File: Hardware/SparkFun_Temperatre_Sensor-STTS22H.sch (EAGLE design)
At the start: 26 parts, among them J1 QWIIC_RIGHT_ANGLE, J2 QWIIC_RIGHT_ANGLE, U2 STTS22H

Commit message: Removes ADDR pin from header
* Routes board
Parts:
- added STANDOFF3: STAND-OFFTIGHT, SparkFun-Hardware:STAND-OFFTIGHT
- J3: device SparkFun-Connectors:CONN_06NO_SILK_NO_POP -> SparkFun-Connectors:CONN_05NO_SILK
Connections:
- net !INT!: now also J3.5; no longer J3.6
- net ADDR: no longer J3.5
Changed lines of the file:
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@@
 <part name="FD4" library="SparkFun-Aesthetics" deviceset="FIDUCIAL" device="1X2"/>
 <part name="LOGO4" library="SparkFun-Aesthetics" deviceset="QWIIC_LOGO" device="_4MM"/>
-<part name="J3" library="SparkFun-Connectors" deviceset="CONN_06" device="NO_SILK_NO_POP"/>
+<part name="J3" library="SparkFun-Connectors" deviceset="CONN_05" device="NO_SILK"/>
 <part name="ADDR" library="SparkFun-Jumpers" deviceset="JUMPER-SMT_3_1-NC_TRACE" device="_SILK" package3d_urn="urn:adsk.eagle:package:39288/1"/>
 <part name="R7" library="SparkFun-Resistors" deviceset="56KOHM" device="" value="56k"/>
@@
 <part name="SUPPLY8" library="SparkFun-PowerSymbols" deviceset="3.3V" device=""/>
 <part name="GND2" library="SparkFun-PowerSymbols" deviceset="GND" device=""/>
+<part name="STANDOFF3" library="SparkFun-Hardware" deviceset="STAND-OFF" device="TIGHT"/>
 </parts>
 <sheets>
@@
 <instance part="FD4" gate="G$1" x="243.84" y="27.94" smashed="yes"/>
 <instance part="LOGO4" gate="G$1" x="180.34" y="40.64" smashed="yes"/>
-<instance part="J3" gate="JP1" x="17.78" y="20.32" smashed="yes">
-<attribute name="VALUE" x="12.7" y="10.414" size="1.778" layer="96" font="vector"/>
-<attribute name="NAME" x="12.7" y="33.528" size="1.778" layer="95" font="vector"/>
+<instance part="J3" gate="G$1" x="15.24" y="20.32" smashed="yes">
+<attribute name="VALUE" x="10.16" y="10.414" size="1.778" layer="96" font="vector"/>
+<attribute name="NAME" x="12.7" y="28.448" size="1.778" layer="95" font="vector"/>
 </instance>
 <instance part="ADDR" gate="G$1" x="25.4" y="101.6" smashed="yes" rot="MR90">
@@
 <attribute name="VALUE" x="104.14" y="96.266" size="1.778" layer="96" font="vector" align="top-center"/>
 </instance>
+<instance part="STANDOFF3" gate="G$1" x="241.3" y="30.48" smashed="yes"/>
 </instances>
 <busses>
@@
 <net name="GND" class="0">
 <segment>
+<pinref part="GND11" gate="1" pin="GND"/>
 <wire x1="22.86" y1="15.24" x2="25.4" y2="15.24" width="0.1524" layer="91"/>
-<pinref part="GND11" gate="1" pin="GND"/>
 <wire x1="25.4" y1="15.24" x2="25.4" y2="12.7" width="0.1524" layer="91"/>
-<pinref part="J3" gate="JP1" pin="1"/>
+<pinref part="J3" gate="G$1" pin="1"/>
 </segment>
 <segment>
@@
 <net name="3.3V" class="0">
 <segment>
+<pinref part="SUPPLY6" gate="G$1" pin="3.3V"/>
 <wire x1="22.86" y1="17.78" x2="25.4" y2="17.78" width="0.1524" layer="91"/>
-<pinref part="SUPPLY6" gate="G$1" pin="3.3V"/>
 <wire x1="25.4" y1="17.78" x2="25.4" y2="38.1" width="0.1524" layer="91"/>
-<pinref part="J3" gate="JP1" pin="2"/>
+<pinref part="J3" gate="G$1" pin="2"/>
 </segment>
 <segment>
@@
 </segment>
 <segment>
-<pinref part="J3" gate="JP1" pin="6"/>
-<wire x1="27.94" y1="27.94" x2="22.86" y2="27.94" width="0.1524" layer="91"/>
-<label x="27.94" y="27.94" size="1.27" layer="95" font="vector" xref="yes"/>
+<wire x1="27.94" y1="25.4" x2="22.86" y2="25.4" width="0.1524" layer="91"/>
+<label x="27.94" y="25.4" size="1.27" layer="95" font="vector" xref="yes"/>
+<pinref part="J3" gate="G$1" pin="5"/>
 </segment>
 </net>
@@
 </segment>
 <segment>
-<pinref part="J3" gate="JP1" pin="5"/>
-<wire x1="27.94" y1="25.4" x2="22.86" y2="25.4" width="0.1524" layer="91"/>
-<label x="27.94" y="25.4" size="1.27" layer="95" font="vector" xref="yes"/>
-</segment>
-<segment>
 <pinref part="ADDR" gate="G$1" pin="2"/>
 <wire x1="22.86" y1="93.98" x2="25.4" y2="93.98" width="0.1524" layer="91"/>
@@
 <wire x1="22.86" y1="22.86" x2="27.94" y2="22.86" width="0.1524" layer="91"/>
 <label x="27.94" y="22.86" size="1.27" layer="95" font="vector" xref="yes"/>
-<pinref part="J3" gate="JP1" pin="4"/>
+<pinref part="J3" gate="G$1" pin="4"/>
 </segment>
 <segment>
@@
 <wire x1="22.86" y1="20.32" x2="27.94" y2="20.32" width="0.1524" layer="91"/>
 <label x="27.94" y="20.32" size="1.27" layer="95" font="vector" xref="yes"/>
-<pinref part="J3" gate="JP1" pin="3"/>
-</segment>
-<segment>
+<pinref part="J3" gate="G$1" pin="3"/>
+</segment>
+<segment>

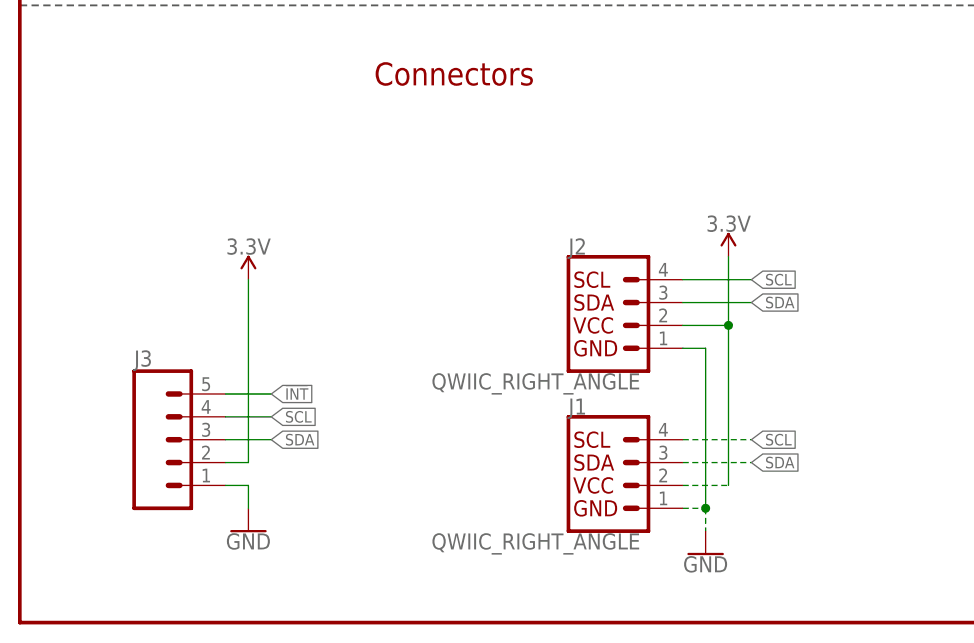
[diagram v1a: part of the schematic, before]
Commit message: Adds silk
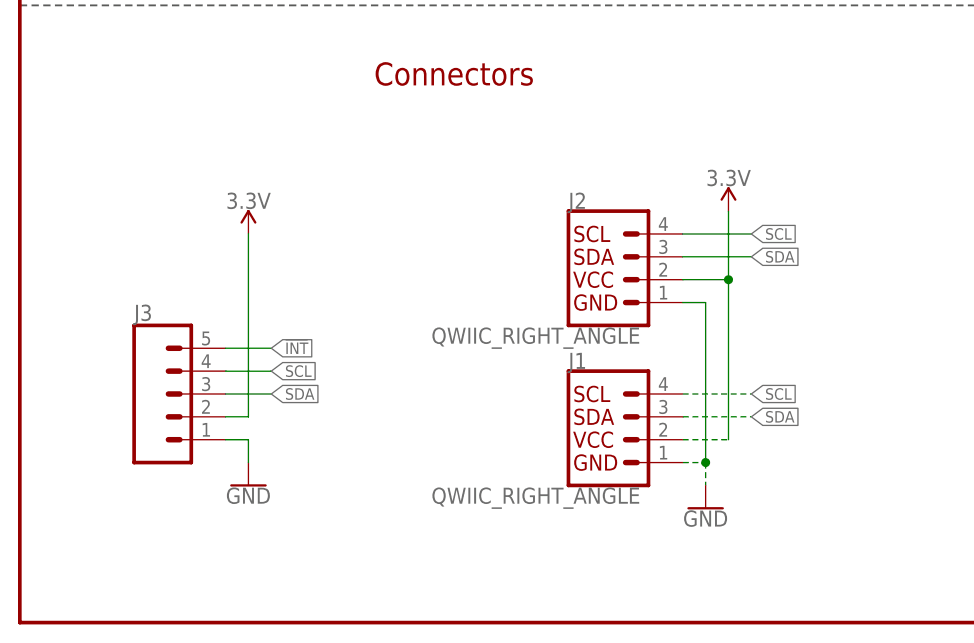
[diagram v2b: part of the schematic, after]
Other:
- moved on the sheet: J1, J2, J3
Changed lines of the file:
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@@
 <attribute name="VALUE" x="167.64" y="132.334" size="1.778" layer="96" font="vector" align="bottom-center"/>
 </instance>
-<instance part="SUPPLY6" gate="G$1" x="25.4" y="38.1" smashed="yes">
-<attribute name="VALUE" x="25.4" y="40.894" size="1.778" layer="96" font="vector" align="bottom-center"/>
-</instance>
-<instance part="GND11" gate="1" x="25.4" y="10.16" smashed="yes">
-<attribute name="VALUE" x="25.4" y="9.906" size="1.778" layer="96" font="vector" align="top-center"/>
+<instance part="SUPPLY6" gate="G$1" x="25.4" y="43.18" smashed="yes">
+<attribute name="VALUE" x="25.4" y="45.974" size="1.778" layer="96" font="vector" align="bottom-center"/>
+</instance>
+<instance part="GND11" gate="1" x="25.4" y="15.24" smashed="yes">
+<attribute name="VALUE" x="25.4" y="14.986" size="1.778" layer="96" font="vector" align="top-center"/>
 </instance>
 <instance part="I2C_PU" gate="G$1" x="167.64" y="121.92" smashed="yes" rot="MR270">
@@
 </instance>
 <instance part="LOGO3" gate="G$1" x="190.5" y="33.02" smashed="yes"/>
-<instance part="J1" gate="G$1" x="66.04" y="15.24" smashed="yes">
-<attribute name="VALUE" x="45.72" y="9.906" size="1.778" layer="96" font="vector" align="top-left"/>
-<attribute name="NAME" x="60.96" y="23.114" size="1.778" layer="95" font="vector"/>
-</instance>
-<instance part="SUPPLY1" gate="G$1" x="78.74" y="40.64" smashed="yes">
-<attribute name="VALUE" x="78.74" y="43.434" size="1.778" layer="96" font="vector" align="bottom-center"/>
-</instance>
-<instance part="GND3" gate="1" x="76.2" y="7.62" smashed="yes">
-<attribute name="VALUE" x="76.2" y="7.366" size="1.778" layer="96" font="vector" align="top-center"/>
-</instance>
-<instance part="J2" gate="G$1" x="66.04" y="33.02" smashed="yes">
-<attribute name="VALUE" x="45.72" y="27.686" size="1.778" layer="96" font="vector" align="top-left"/>
-<attribute name="NAME" x="60.96" y="40.894" size="1.778" layer="95" font="vector"/>
+<instance part="J1" gate="G$1" x="66.04" y="20.32" smashed="yes">
+<attribute name="VALUE" x="45.72" y="14.986" size="1.778" layer="96" font="vector" align="top-left"/>
+<attribute name="NAME" x="60.96" y="28.194" size="1.778" layer="95" font="vector"/>
+</instance>
+<instance part="SUPPLY1" gate="G$1" x="78.74" y="45.72" smashed="yes">
+<attribute name="VALUE" x="78.74" y="48.514" size="1.778" layer="96" font="vector" align="bottom-center"/>
+</instance>
+<instance part="GND3" gate="1" x="76.2" y="12.7" smashed="yes">
+<attribute name="VALUE" x="76.2" y="12.446" size="1.778" layer="96" font="vector" align="top-center"/>
+</instance>
+<instance part="J2" gate="G$1" x="66.04" y="38.1" smashed="yes">
+<attribute name="VALUE" x="45.72" y="32.766" size="1.778" layer="96" font="vector" align="top-left"/>
+<attribute name="NAME" x="60.96" y="45.974" size="1.778" layer="95" font="vector"/>
 </instance>
 <instance part="D1" gate="G$1" x="203.2" y="127" smashed="yes">
@@
 <instance part="FD4" gate="G$1" x="243.84" y="27.94" smashed="yes"/>
 <instance part="LOGO4" gate="G$1" x="180.34" y="40.64" smashed="yes"/>
-<instance part="J3" gate="G$1" x="15.24" y="20.32" smashed="yes">
-<attribute name="VALUE" x="10.16" y="10.414" size="1.778" layer="96" font="vector"/>
-<attribute name="NAME" x="12.7" y="28.448" size="1.778" layer="95" font="vector"/>
+<instance part="J3" gate="G$1" x="15.24" y="25.4" smashed="yes">
+<attribute name="VALUE" x="10.16" y="15.494" size="1.778" layer="96" font="vector"/>
+<attribute name="NAME" x="12.7" y="33.528" size="1.778" layer="95" font="vector"/>
 </instance>
 <instance part="ADDR" gate="G$1" x="25.4" y="101.6" smashed="yes" rot="MR90">
@@
 <segment>
 <pinref part="GND11" gate="1" pin="GND"/>
-<wire x1="22.86" y1="15.24" x2="25.4" y2="15.24" width="0.1524" layer="91"/>
-<wire x1="25.4" y1="15.24" x2="25.4" y2="12.7" width="0.1524" layer="91"/>
+<wire x1="22.86" y1="20.32" x2="25.4" y2="20.32" width="0.1524" layer="91"/>
+<wire x1="25.4" y1="20.32" x2="25.4" y2="17.78" width="0.1524" layer="91"/>
 <pinref part="J3" gate="G$1" pin="1"/>
 </segment>
 <segment>
 <pinref part="J1" gate="G$1" pin="1"/>
-<wire x1="73.66" y1="12.7" x2="76.2" y2="12.7" width="0.1524" layer="91" style="longdash"/>
-<wire x1="76.2" y1="12.7" x2="76.2" y2="10.16" width="0.1524" layer="91" style="longdash"/>
+<wire x1="73.66" y1="17.78" x2="76.2" y2="17.78" width="0.1524" layer="91" style="longdash"/>
+<wire x1="76.2" y1="17.78" x2="76.2" y2="15.24" width="0.1524" layer="91" style="longdash"/>
 <pinref part="GND3" gate="1" pin="GND"/>
 <pinref part="J2" gate="G$1" pin="1"/>
-<wire x1="73.66" y1="30.48" x2="76.2" y2="30.48" width="0.1524" layer="91"/>
-<wire x1="76.2" y1="30.48" x2="76.2" y2="12.7" width="0.1524" layer="91"/>
-<junction x="76.2" y="12.7"/>
+<wire x1="73.66" y1="35.56" x2="76.2" y2="35.56" width="0.1524" layer="91"/>
+<wire x1="76.2" y1="35.56" x2="76.2" y2="17.78" width="0.1524" layer="91"/>
+<junction x="76.2" y="17.78"/>
 </segment>
 <segment>
@@
 <segment>
 <pinref part="SUPPLY6" gate="G$1" pin="3.3V"/>
-<wire x1="22.86" y1="17.78" x2="25.4" y2="17.78" width="0.1524" layer="91"/>
-<wire x1="25.4" y1="17.78" x2="25.4" y2="38.1" width="0.1524" layer="91"/>
+<wire x1="22.86" y1="22.86" x2="25.4" y2="22.86" width="0.1524" layer="91"/>
+<wire x1="25.4" y1="22.86" x2="25.4" y2="43.18" width="0.1524" layer="91"/>
 <pinref part="J3" gate="G$1" pin="2"/>
 </segment>
@@
 <segment>
 <pinref part="J1" gate="G$1" pin="2"/>
-<wire x1="73.66" y1="15.24" x2="78.74" y2="15.24" width="0.1524" layer="91" style="longdash"/>
-<wire x1="78.74" y1="15.24" x2="78.74" y2="33.02" width="0.1524" layer="91"/>
+<wire x1="73.66" y1="20.32" x2="78.74" y2="20.32" width="0.1524" layer="91" style="longdash"/>
+<wire x1="78.74" y1="20.32" x2="78.74" y2="38.1" width="0.1524" layer="91"/>
 <pinref part="SUPPLY1" gate="G$1" pin="3.3V"/>
 <pinref part="J2" gate="G$1" pin="2"/>
-<wire x1="78.74" y1="33.02" x2="78.74" y2="40.64" width="0.1524" layer="91"/>
-<wire x1="73.66" y1="33.02" x2="78.74" y2="33.02" width="0.1524" layer="91"/>
-<junction x="78.74" y="33.02"/>
+<wire x1="78.74" y1="38.1" x2="78.74" y2="45.72" width="0.1524" layer="91"/>
+<wire x1="73.66" y1="38.1" x2="78.74" y2="38.1" width="0.1524" layer="91"/>
+<junction x="78.74" y="38.1"/>
 </segment>
 <segment>
@@
 </segment>
 <segment>
-<wire x1="27.94" y1="25.4" x2="22.86" y2="25.4" width="0.1524" layer="91"/>
-<label x="27.94" y="25.4" size="1.27" layer="95" font="vector" xref="yes"/>
+<wire x1="27.94" y1="30.48" x2="22.86" y2="30.48" width="0.1524" layer="91"/>
+<label x="27.94" y="30.48" size="1.27" layer="95" font="vector" xref="yes"/>
 <pinref part="J3" gate="G$1" pin="5"/>
 </segment>
@@
 </segment>
 <segment>
-<wire x1="22.86" y1="22.86" x2="27.94" y2="22.86" width="0.1524" layer="91"/>
-<label x="27.94" y="22.86" size="1.27" layer="95" font="vector" xref="yes"/>
+<wire x1="22.86" y1="27.94" x2="27.94" y2="27.94" width="0.1524" layer="91"/>
+<label x="27.94" y="27.94" size="1.27" layer="95" font="vector" xref="yes"/>
 <pinref part="J3" gate="G$1" pin="4"/>
 </segment>
 <segment>
 <pinref part="J1" gate="G$1" pin="4"/>
-<wire x1="73.66" y1="20.32" x2="81.28" y2="20.32" width="0.1524" layer="91" style="longdash"/>
-<label x="81.28" y="20.32" size="1.27" layer="95" font="vector" xref="yes"/>
+<wire x1="73.66" y1="25.4" x2="81.28" y2="25.4" width="0.1524" layer="91" style="longdash"/>
+<label x="81.28" y="25.4" size="1.27" layer="95" font="vector" xref="yes"/>
 </segment>
 <segment>
@@
 <segment>
 <pinref part="J2" gate="G$1" pin="4"/>
-<wire x1="73.66" y1="38.1" x2="81.28" y2="38.1" width="0.1524" layer="91"/>
-<label x="81.28" y="38.1" size="1.27" layer="95" font="vector" xref="yes"/>
+<wire x1="73.66" y1="43.18" x2="81.28" y2="43.18" width="0.1524" layer="91"/>
+<label x="81.28" y="43.18" size="1.27" layer="95" font="vector" xref="yes"/>
 </segment>
 </net>
@@
 </segment>
 <segment>
-<wire x1="22.86" y1="20.32" x2="27.94" y2="20.32" width="0.1524" layer="91"/>
-<label x="27.94" y="20.32" size="1.27" layer="95" font="vector" xref="yes"/>
+<wire x1="22.86" y1="25.4" x2="27.94" y2="25.4" width="0.1524" layer="91"/>
+<label x="27.94" y="25.4" size="1.27" layer="95" font="vector" xref="yes"/>
 <pinref part="J3" gate="G$1" pin="3"/>
 </segment>
 <segment>
 <pinref part="J1" gate="G$1" pin="3"/>
-<wire x1="73.66" y1="17.78" x2="81.28" y2="17.78" width="0.1524" layer="91" style="longdash"/>
-<label x="81.28" y="17.78" size="1.27" layer="95" font="vector" xref="yes"/>
+<wire x1="73.66" y1="22.86" x2="81.28" y2="22.86" width="0.1524" layer="91" style="longdash"/>
+<label x="81.28" y="22.86" size="1.27" layer="95" font="vector" xref="yes"/>
 </segment>
 <segment>
@@
 <segment>
 <pinref part="J2" gate="G$1" pin="3"/>
-<wire x1="73.66" y1="35.56" x2="81.28" y2="35.56" width="0.1524" layer="91"/>
-<label x="81.28" y="35.56" size="1.27" layer="95" font="vector" xref="yes"/>
-</segment>
-</net>
+<wire x1="73.66" y1="40.64" x2="81.28" y2="40.64" width="0.1524" layer="91"/>
+<label x="81.28" y="40.64" size="1.27" layer="95" font="vector" xref="yes"/>
+</segment>
+</net>

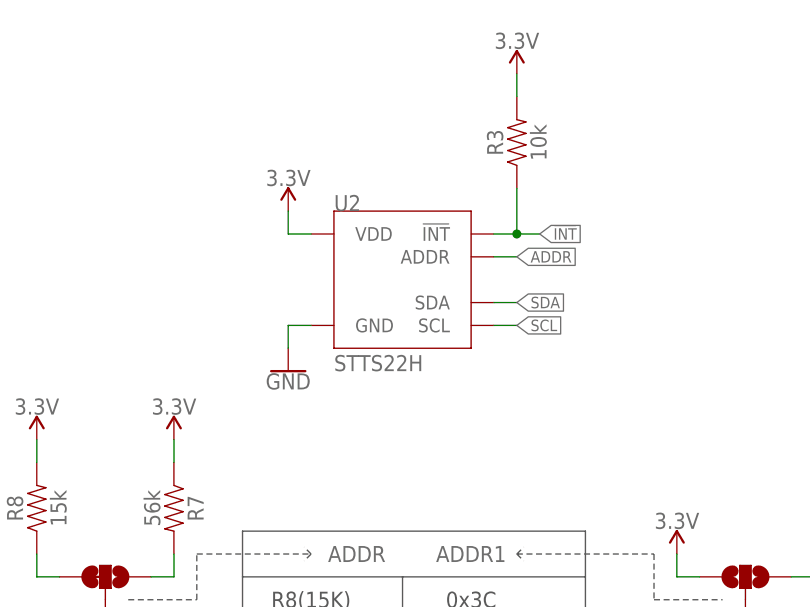
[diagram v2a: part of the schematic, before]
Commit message: Adds decoupling cap which resulted in additional routing
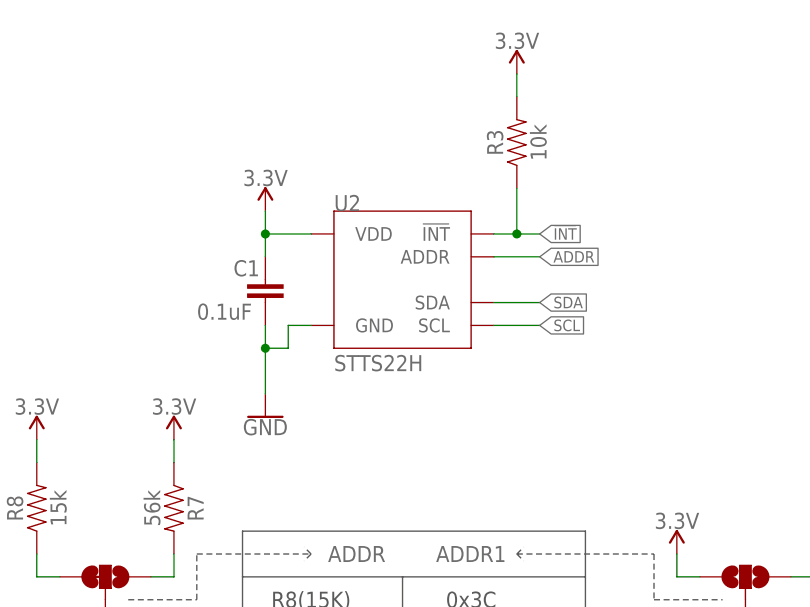
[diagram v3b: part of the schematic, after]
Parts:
- added C1: 0.1uF, SparkFun-Capacitors:0.1UF-0603-25V-(+80/-20%)
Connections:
- net 3.3V: now also C1.1
- net GND: now also C1.2
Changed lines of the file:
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@@
 <part name="GND2" library="SparkFun-PowerSymbols" deviceset="GND" device=""/>
 <part name="STANDOFF3" library="SparkFun-Hardware" deviceset="STAND-OFF" device="TIGHT"/>
+<part name="C1" library="SparkFun-Capacitors" deviceset="0.1UF" device="-0603-25V-(+80/-20%)" value="0.1uF"/>
 </parts>
 <sheets>
@@
 <attribute name="VALUE" x="50.8" y="124.46" size="1.778" layer="96" font="vector"/>
 </instance>
-<instance part="SUPPLY4" gate="G$1" x="45.72" y="142.24" smashed="yes">
-<attribute name="VALUE" x="45.72" y="145.034" size="1.778" layer="96" font="vector" align="bottom-center"/>
-</instance>
-<instance part="GND1" gate="1" x="45.72" y="124.46" smashed="yes">
-<attribute name="VALUE" x="45.72" y="124.206" size="1.778" layer="96" font="vector" align="top-center"/>
+<instance part="SUPPLY4" gate="G$1" x="43.18" y="142.24" smashed="yes">
+<attribute name="VALUE" x="43.18" y="145.034" size="1.778" layer="96" font="vector" align="bottom-center"/>
+</instance>
+<instance part="GND1" gate="1" x="43.18" y="119.38" smashed="yes">
+<attribute name="VALUE" x="43.18" y="119.126" size="1.778" layer="96" font="vector" align="top-center"/>
 </instance>
 <instance part="R3" gate="G$1" x="71.12" y="149.86" smashed="yes" rot="R90">
@@
 </instance>
 <instance part="STANDOFF3" gate="G$1" x="241.3" y="30.48" smashed="yes"/>
+<instance part="C1" gate="G$1" x="43.18" y="132.08" smashed="yes">
+<attribute name="NAME" x="39.624" y="135.001" size="1.778" layer="95" font="vector"/>
+<attribute name="VALUE" x="35.56" y="130.175" size="1.778" layer="96" font="vector"/>
+</instance>
 </instances>
 <busses>
@@
 <segment>
 <pinref part="U2" gate="G$1" pin="GND"/>
+<wire x1="43.18" y1="121.92" x2="43.18" y2="127" width="0.1524" layer="91"/>
+<wire x1="43.18" y1="127" x2="45.72" y2="127" width="0.1524" layer="91"/>
 <wire x1="45.72" y1="127" x2="45.72" y2="129.54" width="0.1524" layer="91"/>
 <wire x1="45.72" y1="129.54" x2="48.26" y2="129.54" width="0.1524" layer="91"/>
 <pinref part="GND1" gate="1" pin="GND"/>
+<pinref part="C1" gate="G$1" pin="2"/>
+<wire x1="43.18" y1="129.54" x2="43.18" y2="127" width="0.1524" layer="91"/>
+<junction x="43.18" y="127"/>
 </segment>
 <segment>
@@
 <segment>
 <pinref part="U2" gate="G$1" pin="VDD"/>
-<wire x1="45.72" y1="142.24" x2="45.72" y2="139.7" width="0.1524" layer="91"/>
-<wire x1="45.72" y1="139.7" x2="48.26" y2="139.7" width="0.1524" layer="91"/>
+<wire x1="43.18" y1="142.24" x2="43.18" y2="139.7" width="0.1524" layer="91"/>
+<wire x1="43.18" y1="139.7" x2="48.26" y2="139.7" width="0.1524" layer="91"/>
 <pinref part="SUPPLY4" gate="G$1" pin="3.3V"/>
+<pinref part="C1" gate="G$1" pin="1"/>
+<wire x1="43.18" y1="137.16" x2="43.18" y2="139.7" width="0.1524" layer="91"/>
+<junction x="43.18" y="139.7"/>
 </segment>
 <segment>
@@
 <segment>
 <pinref part="U2" gate="G$1" pin="ADDR"/>
-<wire x1="71.12" y1="137.16" x2="68.58" y2="137.16" width="0.1524" layer="91"/>
-<label x="71.12" y="137.16" size="1.27" layer="95" font="vector" xref="yes"/>
+<wire x1="73.66" y1="137.16" x2="68.58" y2="137.16" width="0.1524" layer="91"/>
+<label x="73.66" y="137.16" size="1.27" layer="95" font="vector" xref="yes"/>
 </segment>
 <segment>
@@
 <segment>
 <pinref part="U2" gate="G$1" pin="SCL"/>
-<wire x1="71.12" y1="129.54" x2="68.58" y2="129.54" width="0.1524" layer="91"/>
-<label x="71.12" y="129.54" size="1.27" layer="95" font="vector" xref="yes"/>
+<wire x1="73.66" y1="129.54" x2="68.58" y2="129.54" width="0.1524" layer="91"/>
+<label x="73.66" y="129.54" size="1.27" layer="95" font="vector" xref="yes"/>
 </segment>
 <segment>
@@
 <segment>
 <pinref part="U2" gate="G$1" pin="SDA"/>
-<wire x1="71.12" y1="132.08" x2="68.58" y2="132.08" width="0.1524" layer="91"/>
-<label x="71.12" y="132.08" size="1.27" layer="95" font="vector" xref="yes"/>
-</segment>
-<segment>
+<wire x1="73.66" y1="132.08" x2="68.58" y2="132.08" width="0.1524" layer="91"/>
+<label x="73.66" y="132.08" size="1.27" layer="95" font="vector" xref="yes"/>
+</segment>
+<segment>
